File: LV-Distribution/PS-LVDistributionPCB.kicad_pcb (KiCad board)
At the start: 2 copper layers, 149 x 58.5 mm, 49 parts, among them J1 Conn_01x02, J10 Conn_01x02, J11 Conn_01x02, J12 Conn_01x02, J13 Conn_01x02, J14 Conn_01x02, J17 MX150_02x10_RightAngle, J2 Conn_01x02, J3 Conn_01x02, J4 Conn_01x02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

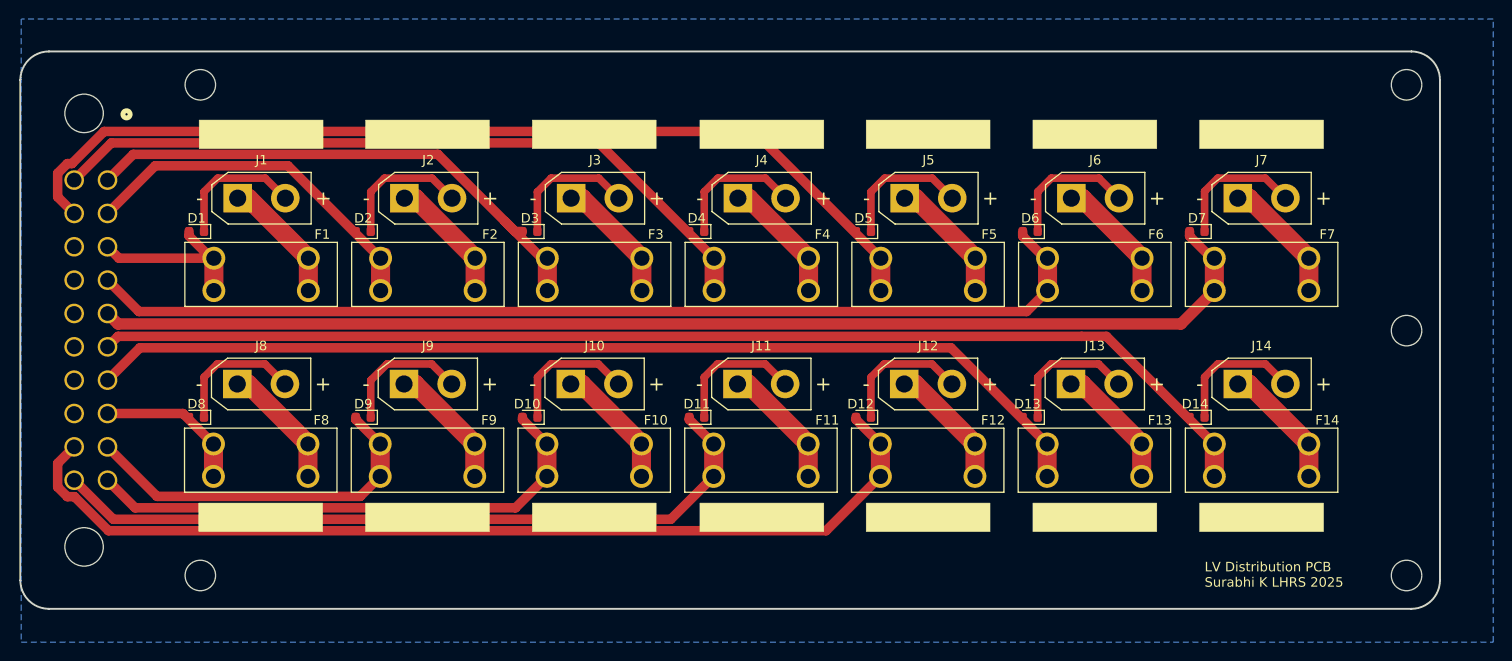
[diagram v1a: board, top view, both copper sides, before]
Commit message: fixed tvs diode on fuseboard
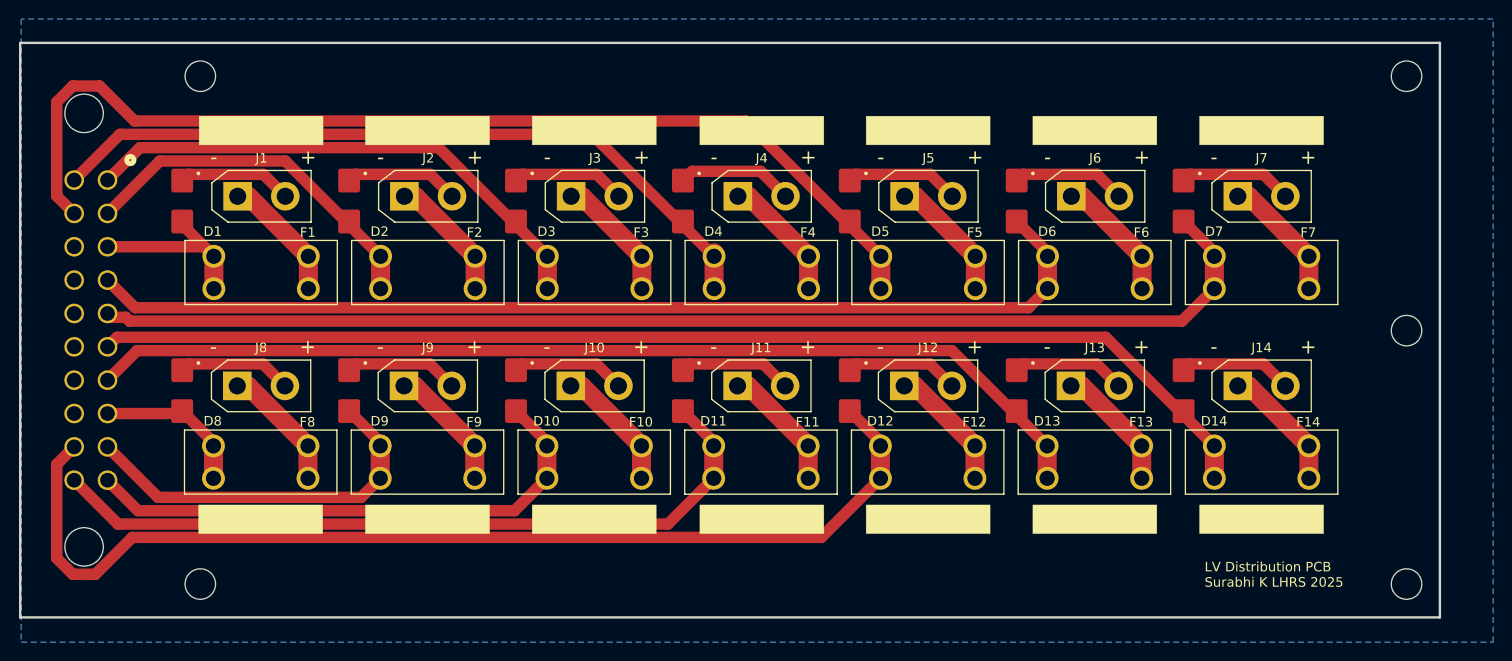
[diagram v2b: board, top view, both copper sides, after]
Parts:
- added G***: LOGO, LOGO, B.Cu at (138.4, 63.8)
- added G***: LOGO, LOGO, B.Cu at (117.2, 64.3)
- D1, D10, D11, D12, D13, D14, D2, D3, D4, D5, D6, D7, D8, D9: footprint Diode_SMD:D_0603_1608Metric -> footprints:D_SMB
- H1, H2, H3, H4, H5: footprint MountingHole:MountingHole_3.2mm_M3 -> footprints:MountingHole_3.2mm_M3
- moved D1 3.53 mm to (102.9, 73.7), turned to -90 degrees
- moved D2 3.53 mm to (120.4, 73.7), turned to -90 degrees
- moved D3 3.51 mm to (137.9, 73.7), turned to -90 degrees
- moved D4 3.51 mm to (155.4, 73.7), turned to -90 degrees
- moved D5 3.51 mm to (173.0, 73.7), turned to -90 degrees
- moved D6 3.50 mm to (190.5, 73.7), turned to -90 degrees
- moved D7 3.50 mm to (208.0, 73.7), turned to -90 degrees
- moved D8 3.18 mm to (102.9, 93.6), turned to -90 degrees
- moved D9 3.17 mm to (120.4, 93.6), turned to -90 degrees
- moved D10 3.16 mm to (137.9, 93.6), turned to -90 degrees
- moved D11 3.15 mm to (155.4, 93.6), turned to -90 degrees
- moved D12 3.15 mm to (173.0, 93.6), turned to -90 degrees
- moved D13 3.14 mm to (190.5, 93.6), turned to -90 degrees
- moved D14 3.14 mm to (208.0, 93.6), turned to -90 degrees
- moved H3 0.90 mm to (104.8, 113.9)
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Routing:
- net GND: track 198.0 -> 167.8 mm
- net P12: track 102.8 -> 112.1 mm
- net P5: track 102.2 -> 110.4 mm
- net P3: track 57.5 -> 55.7 mm
- net P11: track 77.9 -> 79.4 mm
- net P10: track 56.0 -> 57.3 mm
- net P1: track 19.1 -> 20.3 mm
- net P9: track 38.9 -> 40.0 mm
- net P4: track 77.2 -> 78.2 mm
- net P14: track 125.5 -> 124.7 mm
- net P7: track 125.5 -> 126.3 mm
- net P6: track 108.4 -> 109.1 mm
- net P13: track 108.0 -> 107.4 mm
- net P8: track 15.8 -> 16.4 mm
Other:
- board size 149 x 58.5 mm -> 149 x 60.3 mm
